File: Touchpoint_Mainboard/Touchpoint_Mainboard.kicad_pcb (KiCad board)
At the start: 2 copper layers, 58 x 96.4 mm, 95 parts, among them J1 USB4105-GF-A, J2 Conn_01x02, J3 Conn_01x10, J4 Conn_01x32, J5 Conn_01x32, SW1 SW_SPST, SW2 SW_SPST, SW3 SW_SPST, U1 PMW3360DM, U2 USBLC6-2SC6, U3 TLS105B0MBHTSA1, U4 NCP1117-3.3_SOT223, U5 W25Q128JVS, U6 RP2040, U7 DRV2605LDGS, U8 BNO055, U9 HV507PG-G, Y1 ABM8-272-T3, Y2 Crystal

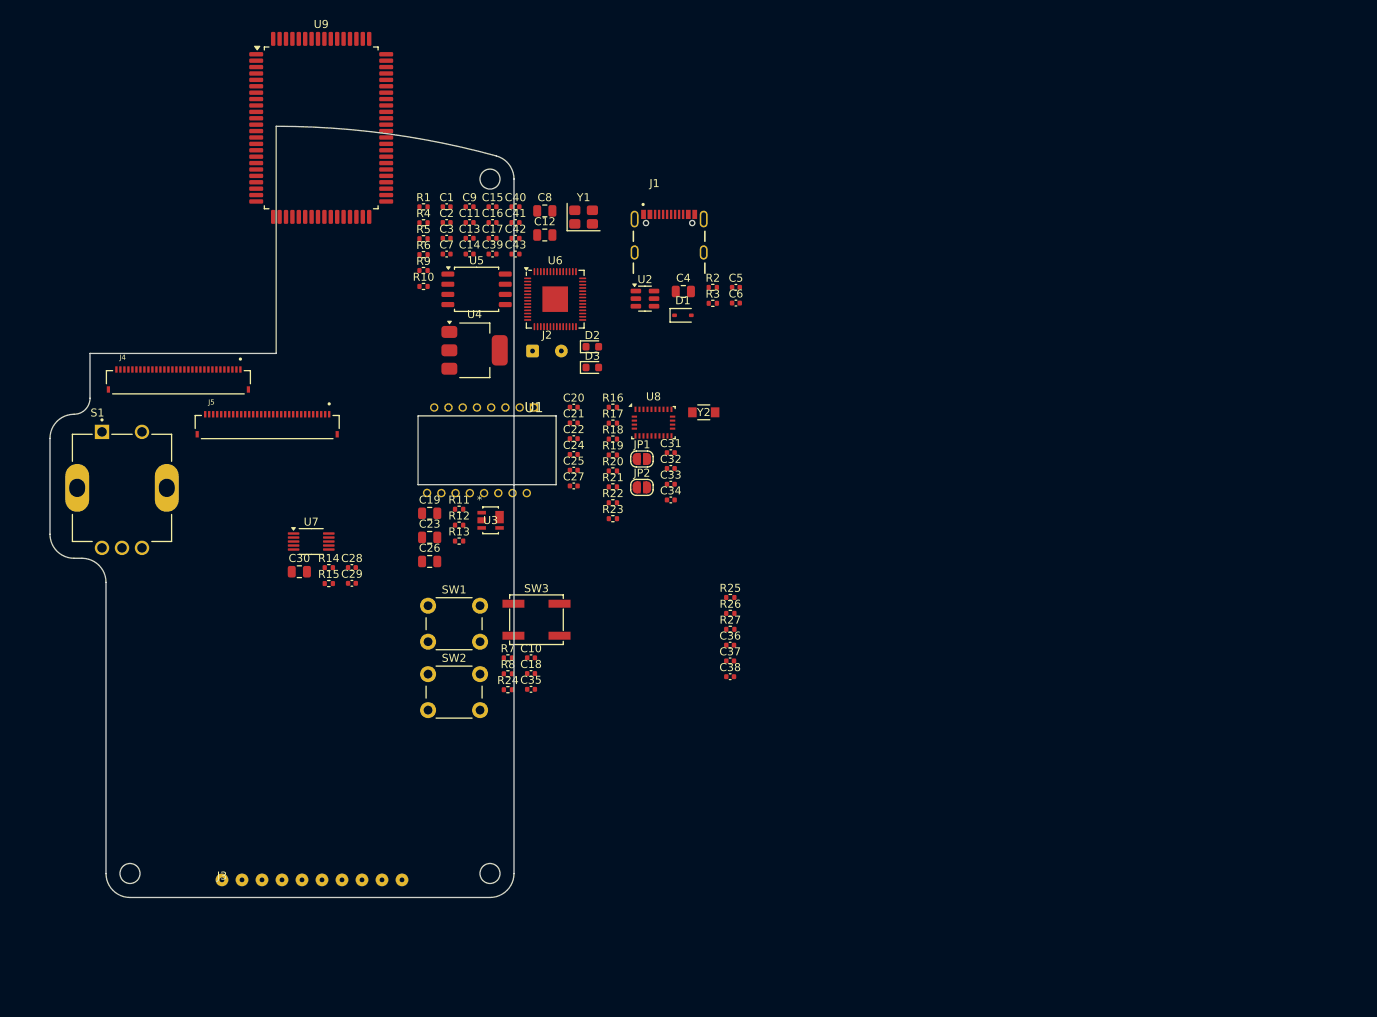
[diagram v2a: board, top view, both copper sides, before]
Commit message: Added 3.3V to interface
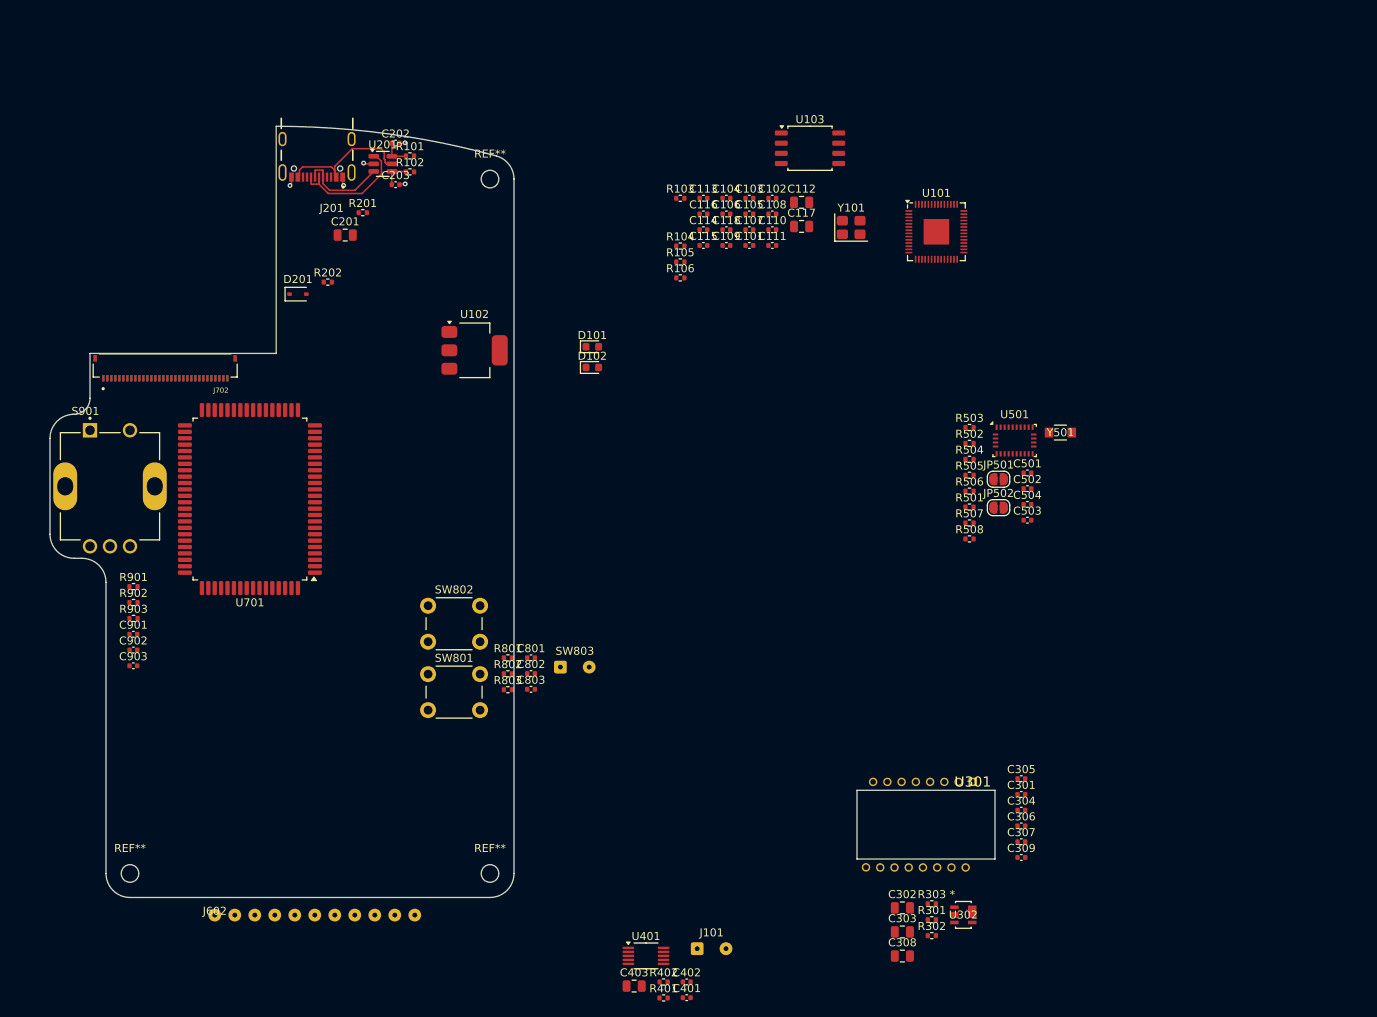
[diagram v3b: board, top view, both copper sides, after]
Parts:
- removed J3: Conn_01x10, Touchpoint:Jumper_Interface_10
- added J602: Conn_01x11, Touchpoint:Jumper_Interface_11, F.Cu at (38.1, 118.6)
- added REF**: MountingHole_2.2mm_M2, MountingHole:MountingHole_2.2mm_M2, F.Cu at (72.5, 26.6)
- added REF**: MountingHole_2.2mm_M2, MountingHole:MountingHole_2.2mm_M2, F.Cu at (27.5, 113.4)
- added REF**: MountingHole_2.2mm_M2, MountingHole:MountingHole_2.2mm_M2, F.Cu at (72.5, 113.4)
- J701: renamed from J4; moved to B.Cu
- SW803: renamed from SW3; footprint Touchpoint:SW_SPST_EVQP0 -> Connector_Wire:SolderWire-0.1sqmm_1x02_P3.6mm_D0.4mm_OD1mm
- moved J101 77.5 mm to (98.4, 122.8)
- moved C302 77.0 mm to (124.0, 117.7)
- moved R301 77.0 mm to (127.7, 119.2)
- moved R302 77.0 mm to (127.7, 121.2)
- moved U302 77.0 mm to (131.7, 118.6)
- moved C303 77.0 mm to (124.0, 120.7)
- moved C308 77.0 mm to (124.0, 123.7)
- moved R303 77.0 mm to (127.7, 117.2)
- moved R901 74.6 mm to (27.9, 77.5)
- moved R902 74.6 mm to (27.9, 79.5)
- moved R903 74.6 mm to (27.9, 81.5)
- moved C901 74.6 mm to (27.9, 83.5)
- moved C902 74.6 mm to (27.9, 85.5)
- moved C903 74.6 mm to (27.9, 87.4)
- moved C309 72.7 mm to (138.9, 111.4)
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- renumbered C39 to C101, C40 to C102, C15 to C103, C9 to C104, C16 to C105, C11 to C106, C17 to C107, C41 to C108, C14 to C109, C42 to C110, C43 to C111, C8 to C112, C1 to C113, C3 to C114, C7 to C115, C2 to C116, C12 to C117, C13 to C118, C4 to C201, C5 to C202, C6 to C203, C21 to C301, C19 to C302, C23 to C303, C22 to C304, C20 to C305, C24 to C306, C25 to C307, C26 to C308, C27 to C309, C29 to C401, C28 to C402, C30 to C403, C31 to C501, C32 to C502, C34 to C503, C33 to C504, C10 to C801, C18 to C802, C35 to C803, C36 to C901, C37 to C902, C38 to C903, D2 to D101, D3 to D102, D1 to D201, J2 to J101, J1 to J201, J5 to J702, JP1 to JP501, JP2 to JP502, R4 to R101, R5 to R102, R1 to R103, R6 to R104, R9 to R105, R10 to R106, R2 to R201, R3 to R202, R12 to R301, R13 to R302, R11 to R303, R15 to R401, R14 to R402, R21 to R501, R17 to R502, R16 to R503, R18 to R504, R19 to R505, R20 to R506, R22 to R507, R23 to R508, R7 to R801, R8 to R802, R24 to R803, R25 to R901, R26 to R902, R27 to R903, S1 to S901, SW2 to SW801, SW1 to SW802, U6 to U101, U4 to U102, U5 to U103, U2 to U201, U1 to U301, U3 to U302, U7 to U401, U8 to U501, U9 to U701, Y1 to Y101, Y2 to Y501
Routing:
- net Net-(D201-A): track 0.00 -> 17.6 mm
- net Net-(J201-DP1): track 0.00 -> 15.7 mm
- net Net-(J201-DN1): track 0.00 -> 11.2 mm
- net GND: track 0.00 -> 4.96 mm, vias 0 -> 5
- net /D-: track 0.00 -> 3.43 mm
- net /D+: track 0.00 -> 3.43 mm
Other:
- outline, holes or cut-outs redrawn

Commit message: Working through mainboard routing
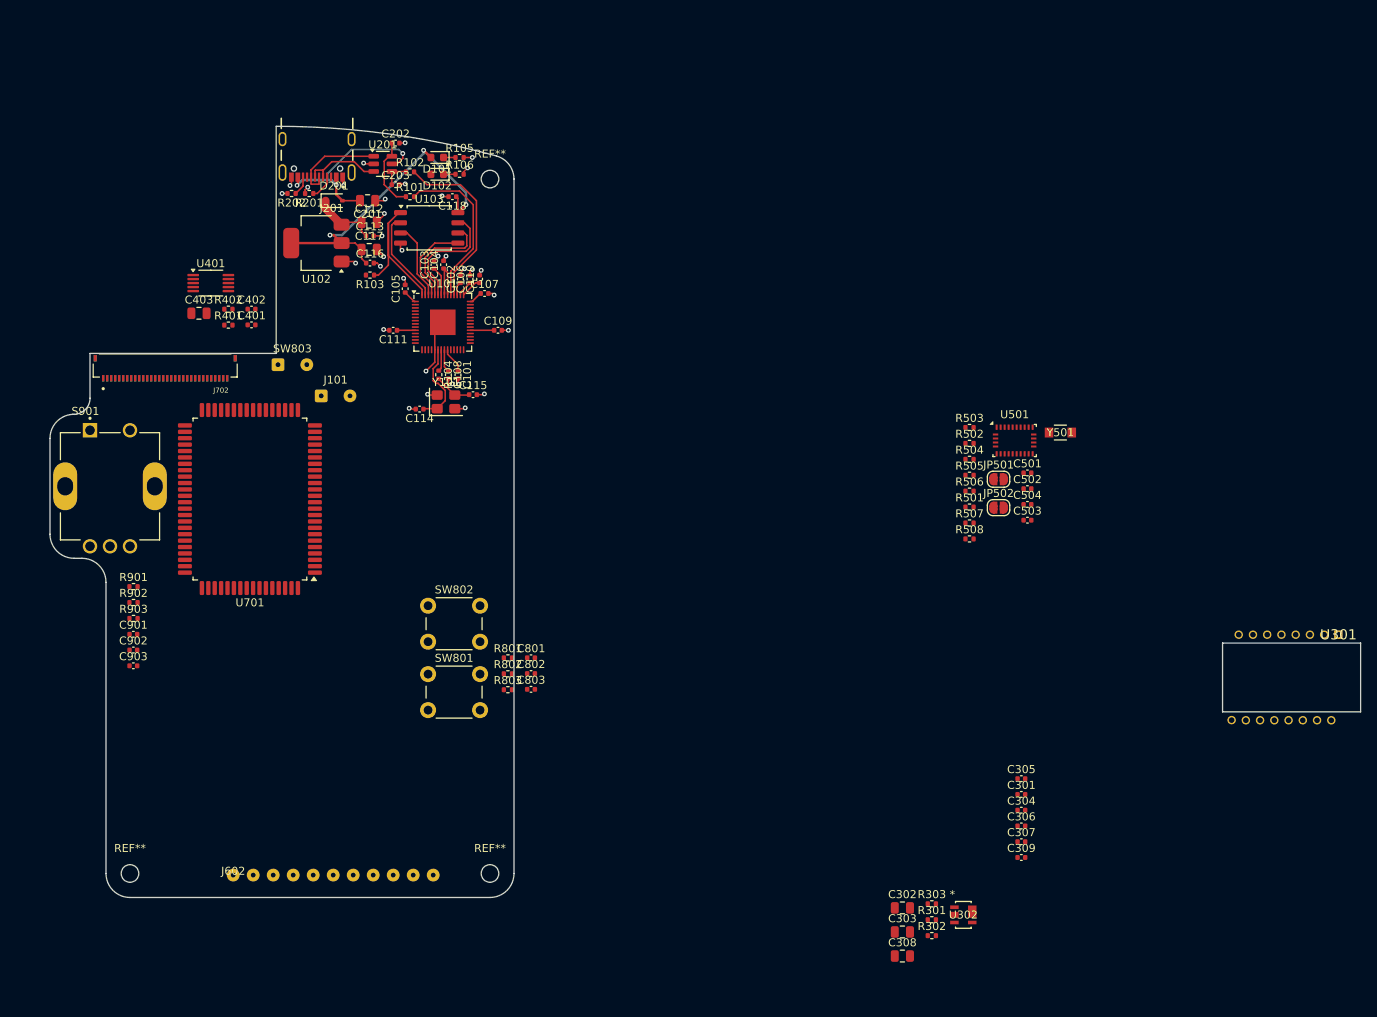
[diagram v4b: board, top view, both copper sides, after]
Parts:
- moved R401 100.2 mm to (39.8, 44.9)
- moved C401 100.2 mm to (42.7, 44.8)
- moved C402 100.2 mm to (42.7, 42.9)
- moved R402 100.2 mm to (39.8, 42.9)
- moved C403 100.2 mm to (36.1, 43.4)
- moved U401 100.2 mm to (37.6, 39.6)
- moved J101 83.6 mm to (51.4, 53.7)
- moved U101 62.7 mm to (66.6, 44.5)
- moved Y101 55.1 mm to (67.0, 54.5)
- moved C117 54.1 mm to (57.4, 35.4)
- moved C112 54.1 mm to (57.4, 32.0)
- moved SW803 51.7 mm to (46.0, 49.8)
- moved U301 49.3 mm to (178.6, 83.5)
- moved U103 48.6 mm to (64.9, 32.7)
- moved C111 48.6 mm to (60.4, 45.5), turned to 180 degrees
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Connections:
- C104 pad 1: +3V3 -> +3.3V
- C105 pad 1: +3V3 -> +3.3V
- C106 pad 1: +3V3 -> +3.3V
- C107 pad 1: +3V3 -> +3.3V
- C108 pad 1: +3V3 -> +3.3V
- C109 pad 1: +3V3 -> +3.3V
- C110 pad 1: +3V3 -> +3.3V
- C111 pad 1: +3V3 -> +3.3V
- C118 pad 1: +3V3 -> +3.3V
- U101 pad 1: +3V3 -> +3.3V
- U101 pad 10: +3V3 -> +3.3V
- U101 pad 22: +3V3 -> +3.3V
- U101 pad 33: +3V3 -> +3.3V
- U101 pad 42: +3V3 -> +3.3V
- U101 pad 43: +3V3 -> +3.3V
- U101 pad 44: +3V3 -> +3.3V
- U101 pad 48: +3V3 -> +3.3V
- U101 pad 49: +3V3 -> +3.3V
- U103 pad 8: +3V3 -> +3.3V
- U701 pad 31: +5V -> VBUS
- U701 pad 32: +5V -> VBUS
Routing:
- net +3.3V: track 0.00 -> 66.0 mm, vias 0 -> 3
- net GND: track 4.96 -> 39.1 mm, vias 5 -> 33
- net Net-(U101-USB_DM): track 0.00 -> 22.2 mm
- net Net-(U101-USB_DP): track 0.00 -> 20.8 mm
- net /QSPI_SS: track 0.00 -> 20.3 mm
- net /QSPI_SD3: track 0.00 -> 15.2 mm
- net /QSPI_SCLK: track 0.00 -> 13.5 mm
- net /QSPI_SD1: track 0.00 -> 11.7 mm
- net /QSPI_SD0: track 0.00 -> 10.7 mm
- net /XIN: track 0.00 -> 10.6 mm
- net /QSPI_SD2: track 0.00 -> 9.65 mm
- net +1V1: track 0.00 -> 8.48 mm
- net VBUS: track 0.00 -> 8.38 mm
- net Net-(D201-A): track 17.6 -> 25.9 mm, vias 0 -> 3
- net /D+: track 3.43 -> 9.15 mm
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
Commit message: Finally finished routing EEOP driver
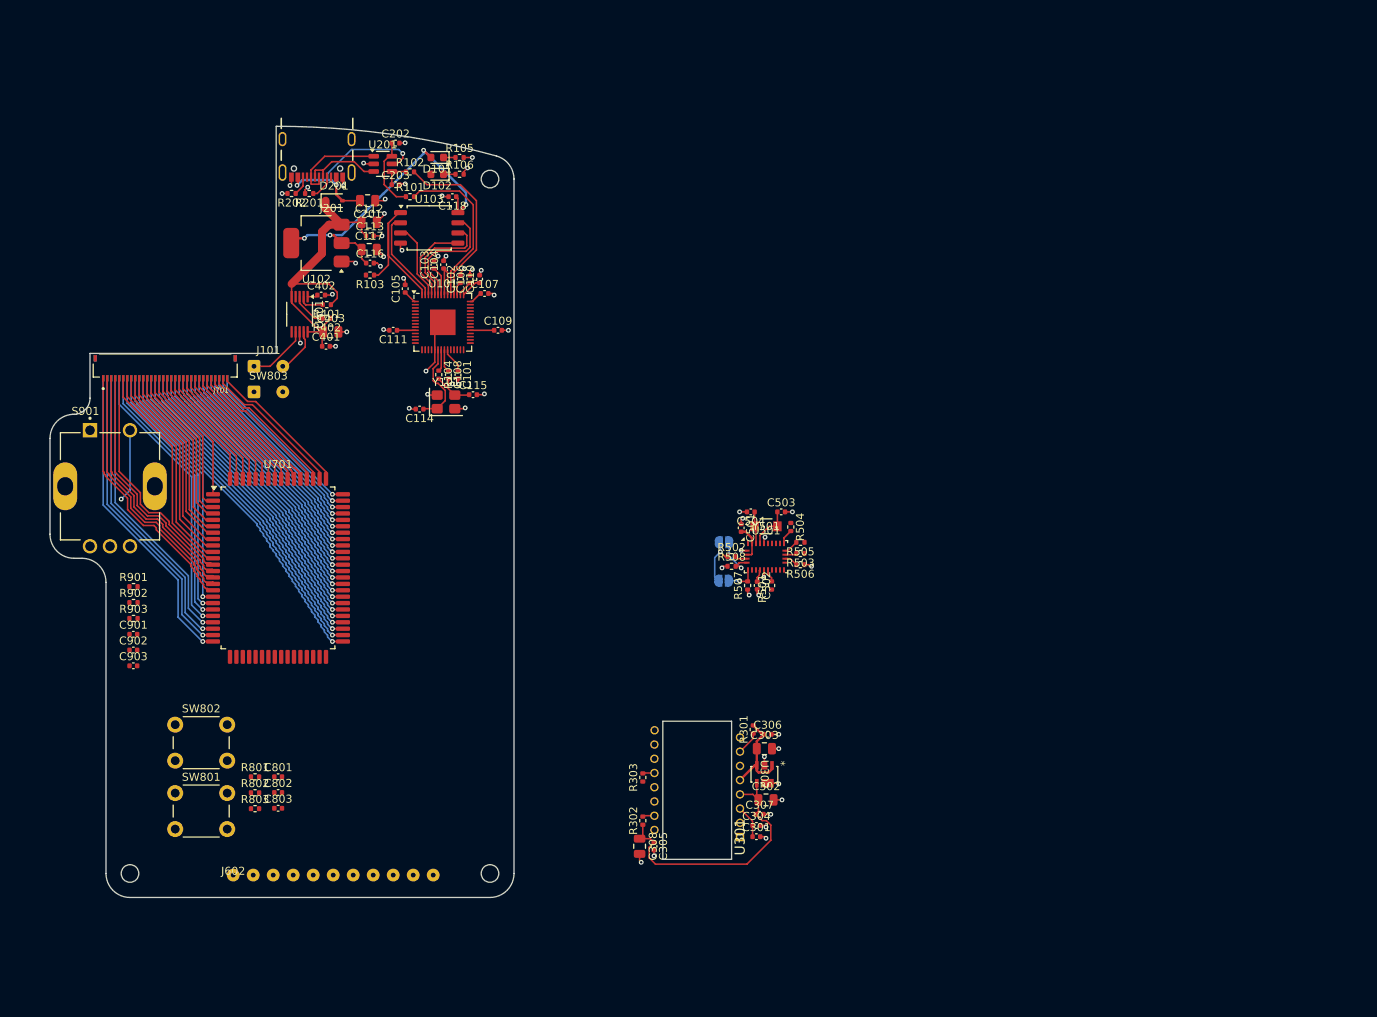
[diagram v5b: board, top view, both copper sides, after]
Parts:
- removed C309: 0.1u, Capacitor_SMD:C_0402_1005Metric
- J701: moved to F.Cu
- J702, JP501, JP502: moved to B.Cu
- moved U301 79.0 mm to (103.8, 108.8), turned to -90 degrees
- moved C305 46.7 mm to (93.0, 110.0), turned to -90 degrees
- moved R303 39.4 mm to (91.6, 101.4), turned to 90 degrees
- moved R302 38.9 mm to (91.6, 106.8), turned to 90 degrees
- moved Y501 38.6 mm to (107.0, 70.0)
- moved JP501 36.6 mm to (101.7, 76.8), turned to 180 degrees
- moved C501 36.4 mm to (103.9, 70.2), turned to -90 degrees
- moved C502 35.9 mm to (105.9, 77.4), turned to -90 degrees
- moved C308 35.6 mm to (91.2, 110.0), turned to -90 degrees
- moved SW801 34.9 mm to (33.1, 103.3)
- moved SW802 34.9 mm to (33.1, 94.8)
- moved C801 34.9 mm to (46.0, 101.3)
- moved C802 34.9 mm to (46.0, 103.3)
- moved C803 34.9 mm to (46.0, 105.2)
- moved R802 34.9 mm to (43.1, 103.3)
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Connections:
- net /DRV2605L/OUTA+ renamed /DRV2605L/OUT+
- net /DRV2605L/OUTA- renamed /DRV2605L/OUT-
- net /EEOP_Driver/OUTB25 renamed /EEOP_Driver/OUT57
- net /EEOP_Driver/OUTB26 renamed /EEOP_Driver/OUT58
- net /EEOP_Driver/OUTB27 renamed /EEOP_Driver/OUT59
- net /EEOP_Driver/OUTB28 renamed /EEOP_Driver/OUT60
- net /EEOP_Driver/OUTB29 renamed /EEOP_Driver/OUT61
- net /EEOP_Driver/OUTB30 renamed /EEOP_Driver/OUT62
- net /EEOP_Driver/OUTB31 renamed /EEOP_Driver/OUT63
- net /EEOP_Driver/OUTB32 renamed /EEOP_Driver/OUT64
- net /XOUTA renamed /XOUT
- J701 pad 1: /EEOP_Driver/OUTA1 -> /EEOP_Driver/OUT56
- J701 pad 10: /EEOP_Driver/OUTA10 -> /EEOP_Driver/OUT47
- J701 pad 11: /EEOP_Driver/OUTA11 -> /EEOP_Driver/OUT46
- J701 pad 12: /EEOP_Driver/OUTA12 -> /EEOP_Driver/OUT45
- J701 pad 13: /EEOP_Driver/OUTA13 -> /EEOP_Driver/OUT44
- J701 pad 14: /EEOP_Driver/OUTA14 -> /EEOP_Driver/OUT43
- J701 pad 15: /EEOP_Driver/OUTA15 -> /EEOP_Driver/OUT42
- J701 pad 16: /EEOP_Driver/OUTA16 -> /EEOP_Driver/OUT41
- J701 pad 17: /EEOP_Driver/OUTA17 -> /EEOP_Driver/OUT40
- J701 pad 18: /EEOP_Driver/OUTA18 -> /EEOP_Driver/OUT39
- J701 pad 19: /EEOP_Driver/OUTA19 -> /EEOP_Driver/OUT38
- J701 pad 2: /EEOP_Driver/OUTA2 -> /EEOP_Driver/OUT55
- J701 pad 20: /EEOP_Driver/OUTA20 -> /EEOP_Driver/OUT37
- J701 pad 21: /EEOP_Driver/OUTA21 -> /EEOP_Driver/OUT36
- J701 pad 22: /EEOP_Driver/OUTA22 -> /EEOP_Driver/OUT35
- J701 pad 23: /EEOP_Driver/OUTA23 -> /EEOP_Driver/OUT34
- J701 pad 24: /EEOP_Driver/OUTA24 -> /EEOP_Driver/OUT33
- J701 pad 25: /EEOP_Driver/OUTA25 -> /EEOP_Driver/OUT32
- J701 pad 26: /EEOP_Driver/OUTA26 -> /EEOP_Driver/OUT31
- J701 pad 27: /EEOP_Driver/OUTA27 -> /EEOP_Driver/OUT30
- J701 pad 28: /EEOP_Driver/OUTA28 -> /EEOP_Driver/OUT29
- J701 pad 29: /EEOP_Driver/OUTA29 -> /EEOP_Driver/OUT28
- J701 pad 3: /EEOP_Driver/OUTA3 -> /EEOP_Driver/OUT54
- J701 pad 30: /EEOP_Driver/OUTA30 -> /EEOP_Driver/OUT27
- J701 pad 31: /EEOP_Driver/OUTA31 -> /EEOP_Driver/OUT26
- J701 pad 32: /EEOP_Driver/OUTA32 -> /EEOP_Driver/OUT25
- J701 pad 4: /EEOP_Driver/OUTA4 -> /EEOP_Driver/OUT53
- J701 pad 5: /EEOP_Driver/OUTA5 -> /EEOP_Driver/OUT52
- J701 pad 6: /EEOP_Driver/OUTA6 -> /EEOP_Driver/OUT51
- J701 pad 7: /EEOP_Driver/OUTA7 -> /EEOP_Driver/OUT50
- J701 pad 8: /EEOP_Driver/OUTA8 -> /EEOP_Driver/OUT49
- J701 pad 9: /EEOP_Driver/OUTA9 -> /EEOP_Driver/OUT48
- J702 pad 1: /EEOP_Driver/OUTB1 -> /EEOP_Driver/OUT24
- J702 pad 10: /EEOP_Driver/OUTB10 -> /EEOP_Driver/OUT15
- J702 pad 11: /EEOP_Driver/OUTB11 -> /EEOP_Driver/OUT14
- J702 pad 12: /EEOP_Driver/OUTB12 -> /EEOP_Driver/OUT13
- J702 pad 13: /EEOP_Driver/OUTB13 -> /EEOP_Driver/OUT12
- J702 pad 14: /EEOP_Driver/OUTB14 -> /EEOP_Driver/OUT11
- J702 pad 15: /EEOP_Driver/OUTB15 -> /EEOP_Driver/OUT10
- J702 pad 16: /EEOP_Driver/OUTB16 -> /EEOP_Driver/OUT9
- J702 pad 17: /EEOP_Driver/OUTB17 -> /EEOP_Driver/OUT8
- J702 pad 18: /EEOP_Driver/OUTB18 -> /EEOP_Driver/OUT7
- J702 pad 19: /EEOP_Driver/OUTB19 -> /EEOP_Driver/OUT6
- J702 pad 2: /EEOP_Driver/OUTB2 -> /EEOP_Driver/OUT23
- J702 pad 20: /EEOP_Driver/OUTB20 -> /EEOP_Driver/OUT5
- J702 pad 21: /EEOP_Driver/OUTB21 -> /EEOP_Driver/OUT4
- J702 pad 22: /EEOP_Driver/OUTB22 -> /EEOP_Driver/OUT3
- J702 pad 23: /EEOP_Driver/OUTB23 -> /EEOP_Driver/OUT2
- J702 pad 24: /EEOP_Driver/OUTB24 -> /EEOP_Driver/OUT1
- J702 pad 3: /EEOP_Driver/OUTB3 -> /EEOP_Driver/OUT22
- J702 pad 4: /EEOP_Driver/OUTB4 -> /EEOP_Driver/OUT21
- J702 pad 5: /EEOP_Driver/OUTB5 -> /EEOP_Driver/OUT20
- J702 pad 6: /EEOP_Driver/OUTB6 -> /EEOP_Driver/OUT19
- J702 pad 7: /EEOP_Driver/OUTB7 -> /EEOP_Driver/OUT18
- J702 pad 8: /EEOP_Driver/OUTB8 -> /EEOP_Driver/OUT17
- J702 pad 9: /EEOP_Driver/OUTB9 -> /EEOP_Driver/OUT16
- U701 pad 1: /EEOP_Driver/OUTB9 -> /EEOP_Driver/OUT41
- U701 pad 10: /EEOP_Driver/OUTB18 -> /EEOP_Driver/OUT50
- U701 pad 11: /EEOP_Driver/OUTB19 -> /EEOP_Driver/OUT51
- U701 pad 12: /EEOP_Driver/OUTB20 -> /EEOP_Driver/OUT52
- U701 pad 13: /EEOP_Driver/OUTB21 -> /EEOP_Driver/OUT53
- U701 pad 14: /EEOP_Driver/OUTB22 -> /EEOP_Driver/OUT54
- U701 pad 15: /EEOP_Driver/OUTB23 -> /EEOP_Driver/OUT55
- U701 pad 16: /EEOP_Driver/OUTB24 -> /EEOP_Driver/OUT56
- U701 pad 2: /EEOP_Driver/OUTB10 -> /EEOP_Driver/OUT42
- U701 pad 3: /EEOP_Driver/OUTB11 -> /EEOP_Driver/OUT43
- U701 pad 4: /EEOP_Driver/OUTB12 -> /EEOP_Driver/OUT44
- U701 pad 41: /EEOP_Driver/OUTA1 -> /EEOP_Driver/OUT1
- U701 pad 42: /EEOP_Driver/OUTA2 -> /EEOP_Driver/OUT2
- U701 pad 43: /EEOP_Driver/OUTA3 -> /EEOP_Driver/OUT3
- U701 pad 44: /EEOP_Driver/OUTA4 -> /EEOP_Driver/OUT4
- U701 pad 45: /EEOP_Driver/OUTA5 -> /EEOP_Driver/OUT5
- U701 pad 46: /EEOP_Driver/OUTA6 -> /EEOP_Driver/OUT6
- U701 pad 47: /EEOP_Driver/OUTA7 -> /EEOP_Driver/OUT7
- U701 pad 48: /EEOP_Driver/OUTA8 -> /EEOP_Driver/OUT8
- U701 pad 49: /EEOP_Driver/OUTA9 -> /EEOP_Driver/OUT9
- U701 pad 5: /EEOP_Driver/OUTB13 -> /EEOP_Driver/OUT45
- U701 pad 50: /EEOP_Driver/OUTA10 -> /EEOP_Driver/OUT10
- U701 pad 51: /EEOP_Driver/OUTA11 -> /EEOP_Driver/OUT11
- U701 pad 52: /EEOP_Driver/OUTA12 -> /EEOP_Driver/OUT12
- U701 pad 53: /EEOP_Driver/OUTA13 -> /EEOP_Driver/OUT13
- U701 pad 54: /EEOP_Driver/OUTA14 -> /EEOP_Driver/OUT14
- U701 pad 55: /EEOP_Driver/OUTA15 -> /EEOP_Driver/OUT15
- U701 pad 56: /EEOP_Driver/OUTA16 -> /EEOP_Driver/OUT16
- U701 pad 57: /EEOP_Driver/OUTA17 -> /EEOP_Driver/OUT17
- U701 pad 58: /EEOP_Driver/OUTA18 -> /EEOP_Driver/OUT18
- U701 pad 59: /EEOP_Driver/OUTA19 -> /EEOP_Driver/OUT19
- U701 pad 6: /EEOP_Driver/OUTB14 -> /EEOP_Driver/OUT46
- U701 pad 60: /EEOP_Driver/OUTA20 -> /EEOP_Driver/OUT20
- U701 pad 61: /EEOP_Driver/OUTA21 -> /EEOP_Driver/OUT21
- U701 pad 62: /EEOP_Driver/OUTA22 -> /EEOP_Driver/OUT22
- U701 pad 63: /EEOP_Driver/OUTA23 -> /EEOP_Driver/OUT23
- U701 pad 64: /EEOP_Driver/OUTA24 -> /EEOP_Driver/OUT24
- U701 pad 65: /EEOP_Driver/OUTA25 -> /EEOP_Driver/OUT25
- U701 pad 66: /EEOP_Driver/OUTA26 -> /EEOP_Driver/OUT26
- U701 pad 67: /EEOP_Driver/OUTA27 -> /EEOP_Driver/OUT27
- U701 pad 68: /EEOP_Driver/OUTA28 -> /EEOP_Driver/OUT28
- U701 pad 69: /EEOP_Driver/OUTA29 -> /EEOP_Driver/OUT29
- U701 pad 7: /EEOP_Driver/OUTB15 -> /EEOP_Driver/OUT47
- U701 pad 70: /EEOP_Driver/OUTA30 -> /EEOP_Driver/OUT30
- U701 pad 71: /EEOP_Driver/OUTA31 -> /EEOP_Driver/OUT31
- U701 pad 72: /EEOP_Driver/OUTA32 -> /EEOP_Driver/OUT32
- U701 pad 73: /EEOP_Driver/OUTB1 -> /EEOP_Driver/OUT33
- U701 pad 74: /EEOP_Driver/OUTB2 -> /EEOP_Driver/OUT34
- U701 pad 75: /EEOP_Driver/OUTB3 -> /EEOP_Driver/OUT35
- U701 pad 76: /EEOP_Driver/OUTB4 -> /EEOP_Driver/OUT36
- U701 pad 77: /EEOP_Driver/OUTB5 -> /EEOP_Driver/OUT37
- U701 pad 78: /EEOP_Driver/OUTB6 -> /EEOP_Driver/OUT38
- U701 pad 79: /EEOP_Driver/OUTB7 -> /EEOP_Driver/OUT39
- U701 pad 8: /EEOP_Driver/OUTB16 -> /EEOP_Driver/OUT48
- U701 pad 80: /EEOP_Driver/OUTB8 -> /EEOP_Driver/OUT40
- U701 pad 9: /EEOP_Driver/OUTB17 -> /EEOP_Driver/OUT49
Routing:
- net /EEOP_Driver/OUT1: track 0.00 -> 44.6 mm, vias 0 -> 1
- net /EEOP_Driver/OUT2: track 0.00 -> 43.6 mm, vias 0 -> 1
- net /EEOP_Driver/OUT3: track 0.00 -> 42.6 mm, vias 0 -> 1
- net /EEOP_Driver/OUT4: track 0.00 -> 41.6 mm, vias 0 -> 1
- net /EEOP_Driver/OUT5: track 0.00 -> 40.6 mm, vias 0 -> 1
- net /EEOP_Driver/OUT6: track 0.00 -> 39.5 mm, vias 0 -> 1
- net /EEOP_Driver/OUT64: track 0.00 -> 39.4 mm, vias 0 -> 1
- net /EEOP_Driver/OUT7: track 0.00 -> 38.5 mm, vias 0 -> 1
- net /EEOP_Driver/OUT63: track 0.00 -> 38.4 mm, vias 0 -> 1
- net /EEOP_Driver/OUT8: track 0.00 -> 37.5 mm, vias 0 -> 1
- net /EEOP_Driver/OUT62: track 0.00 -> 37.4 mm, vias 0 -> 1
- net /EEOP_Driver/OUT9: track 0.00 -> 36.5 mm, vias 0 -> 1
- net /EEOP_Driver/OUT61: track 0.00 -> 36.3 mm, vias 0 -> 1
- net /EEOP_Driver/OUT10: track 0.00 -> 35.5 mm, vias 0 -> 1
- net /EEOP_Driver/OUT60: track 0.00 -> 35.3 mm, vias 0 -> 1
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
